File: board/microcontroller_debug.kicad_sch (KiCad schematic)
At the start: 1 part, among them J401 DBG

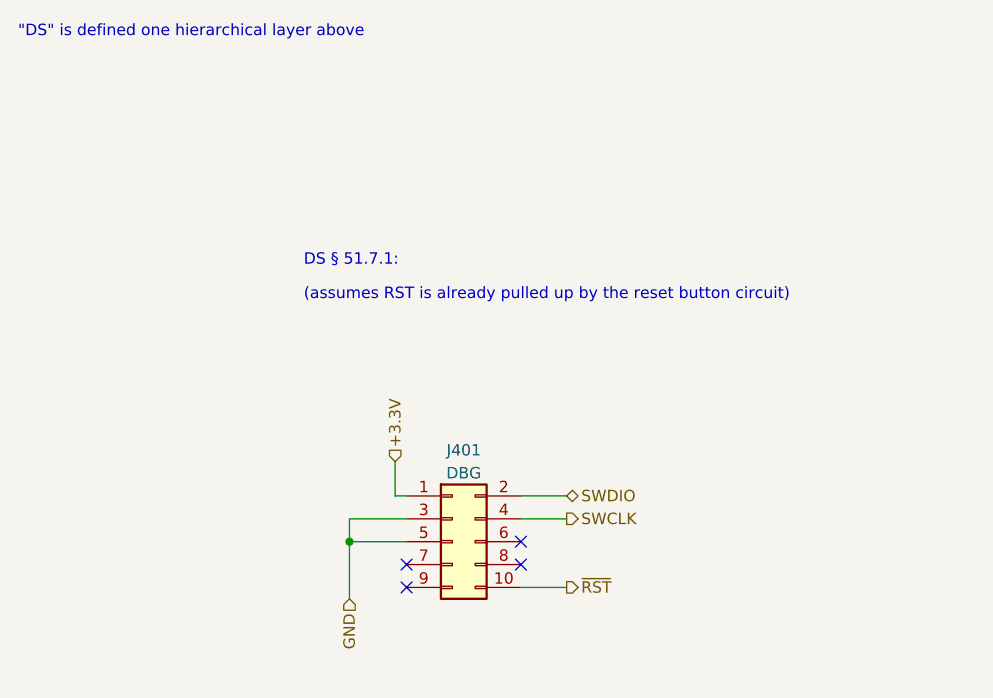
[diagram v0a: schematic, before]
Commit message: redo board with STM32G0B0CET
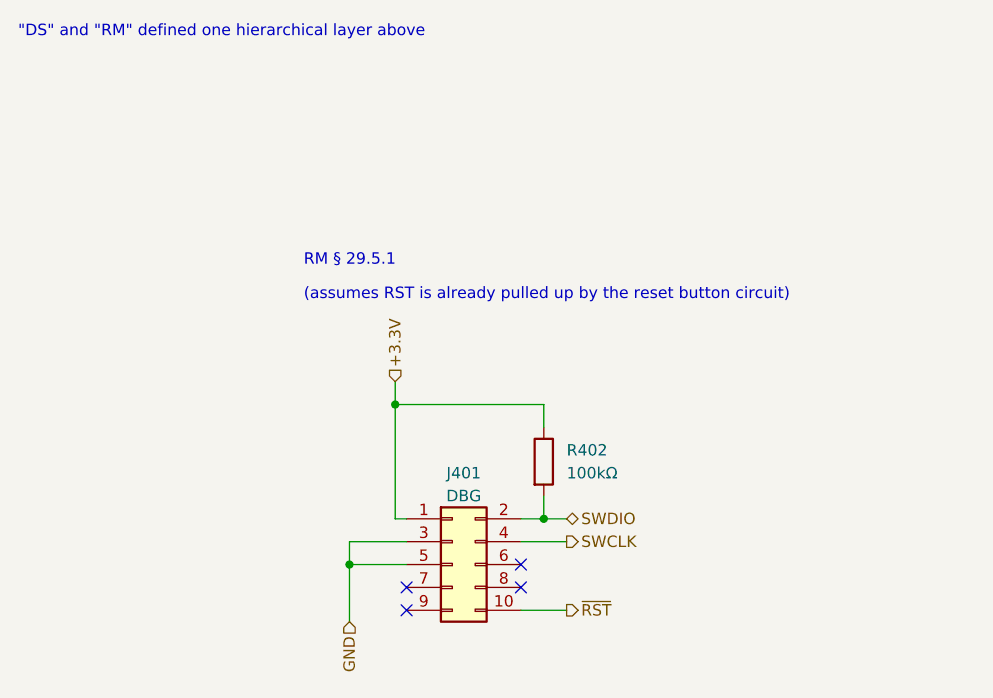
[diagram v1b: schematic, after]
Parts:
- added R402: 100kΩ, Resistor_SMD:R_0402_1005Metric, symbol Device:R
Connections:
- net +3.3V: now also R402.1
- net SWDIO: now also R402.2
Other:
- note added: ""DS" and "RM" defined one hierarchical layer above"
- note added: "RM § 29.5.1"
- note removed: ""DS" is defined one hierarchical layer above"
- note removed: "DS § 51.7.1:"
- moved on the sheet: J401
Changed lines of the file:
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@@
 (kicad_sch (version 20230121) (generator eeschema)
   (paper "A4")
-  (junction (at 50.8 72.39) (diameter 0) (color 0 0 0 0)
+  (junction (at 72.39 69.85) (diameter 0) (color 0 0 0 0)
   )
+  (junction (at 55.88 57.15) (diameter 0) (color 0 0 0 0)
+  )
+  (junction (at 50.8 74.93) (diameter 0) (color 0 0 0 0)
+  )
+  (no_connect (at 57.15 80.01))
+  (no_connect (at 69.85 77.47))
+  (no_connect (at 69.85 74.93))
   (no_connect (at 57.15 77.47))
-  (no_connect (at 69.85 74.93))
-  (no_connect (at 69.85 72.39))
-  (no_connect (at 57.15 74.93))
-  (wire (pts (xy 50.8 72.39) (xy 57.15 72.39))
+  (wire (pts (xy 72.39 57.15) (xy 72.39 59.69))
     (stroke (width 0) (type default))
   )
-  (wire (pts (xy 55.88 67.31) (xy 55.88 63.5))
+  (wire (pts (xy 50.8 74.93) (xy 57.15 74.93))
     (stroke (width 0) (type default))
   )
-  (wire (pts (xy 69.85 77.47) (xy 74.93 77.47))
+  (wire (pts (xy 55.88 57.15) (xy 72.39 57.15))
     (stroke (width 0) (type default))
   )
-  (wire (pts (xy 69.85 69.85) (xy 74.93 69.85))
+  (wire (pts (xy 55.88 54.61) (xy 55.88 57.15))
     (stroke (width 0) (type default))
   )
-  (wire (pts (xy 69.85 67.31) (xy 74.93 67.31))
+  (wire (pts (xy 69.85 80.01) (xy 74.93 80.01))
     (stroke (width 0) (type default))
   )
-  (wire (pts (xy 57.15 69.85) (xy 50.8 69.85))
+  (wire (pts (xy 69.85 72.39) (xy 74.93 72.39))
     (stroke (width 0) (type default))
   )
-  (wire (pts (xy 57.15 67.31) (xy 55.88 67.31))
+  (wire (pts (xy 69.85 69.85) (xy 72.39 69.85))
     (stroke (width 0) (type default))
   )
-  (wire (pts (xy 50.8 69.85) (xy 50.8 72.39))
+  (wire (pts (xy 55.88 57.15) (xy 55.88 69.85))
     (stroke (width 0) (type default))
   )
-  (wire (pts (xy 50.8 72.39) (xy 50.8 78.74))
+  (wire (pts (xy 57.15 72.39) (xy 50.8 72.39))
     (stroke (width 0) (type default))
   )
-  (text "DS § 51.7.1:" (at 45.72 41.91 0)
+  (wire (pts (xy 57.15 69.85) (xy 55.88 69.85))
+    (stroke (width 0) (type default))
+  )
+  (wire (pts (xy 72.39 69.85) (xy 74.93 69.85))
+    (stroke (width 0) (type default))
+  )
+  (wire (pts (xy 50.8 72.39) (xy 50.8 74.93))
+    (stroke (width 0) (type default))
+  )
+  (wire (pts (xy 72.39 67.31) (xy 72.39 69.85))
+    (stroke (width 0) (type default))
+  )
+  (wire (pts (xy 50.8 74.93) (xy 50.8 81.28))
+    (stroke (width 0) (type default))
+  )
+  (text "RM § 29.5.1" (at 45.72 41.91 0)
     (effects (font (size 1.27 1.27)) (justify left bottom))
   )
@@
     (effects (font (size 1.27 1.27)) (justify left bottom))
   )
-  (text "\"DS\" is defined one hierarchical layer above" (at 13.97 16.51 0)
+  (text "\"DS\" and \"RM\" defined one hierarchical layer above"
+    (at 13.97 16.51 0)
     (effects (font (size 1.27 1.27)) (justify left bottom))
   )
-  (hierarchical_label "SWDIO" (shape bidirectional) (at 74.93 67.31 0) (fields_autoplaced)
+  (hierarchical_label "SWDIO" (shape bidirectional) (at 74.93 69.85 0) (fields_autoplaced)
     (effects (font (size 1.27 1.27)) (justify left))
   )
-  (hierarchical_label "SWCLK" (shape output) (at 74.93 69.85 0) (fields_autoplaced)
+  (hierarchical_label "SWCLK" (shape output) (at 74.93 72.39 0) (fields_autoplaced)
     (effects (font (size 1.27 1.27)) (justify left))
   )
-  (hierarchical_label "~{RST}" (shape output) (at 74.93 77.47 0) (fields_autoplaced)
+  (hierarchical_label "~{RST}" (shape output) (at 74.93 80.01 0) (fields_autoplaced)
     (effects (font (size 1.27 1.27)) (justify left))
   )
-  (hierarchical_label "+3.3V" (shape input) (at 55.88 63.5 90) (fields_autoplaced)
+  (hierarchical_label "+3.3V" (shape input) (at 55.88 54.61 90) (fields_autoplaced)
     (effects (font (size 1.27 1.27)) (justify left))
   )
-  (hierarchical_label "GND" (shape input) (at 50.8 78.74 270) (fields_autoplaced)
+  (hierarchical_label "GND" (shape input) (at 50.8 81.28 270) (fields_autoplaced)
     (effects (font (size 1.27 1.27)) (justify right))
   )
-  (symbol (lib_id "Connector_Generic:Conn_02x05_Odd_Even") (at 62.23 72.39 0) (unit 1)
+  (symbol (lib_id "Device:R") (at 72.39 63.5 0) (unit 1)
     (in_bom yes) (on_board yes) (dnp no) (fields_autoplaced)
-    (property "Reference" "J401" (at 63.5 62.23 0)
+    (property "Reference" "R402" (at 74.93 62.23 0)
+      (effects (font (size 1.27 1.27)) (justify left))
+    )
+    (property "Value" "100kΩ" (at 74.93 64.77 0)
+      (effects (font (size 1.27 1.27)) (justify left))
+    )
+    (property "Footprint" "Resistor_SMD:R_0402_1005Metric" (at 70.612 63.5 90)
+      (effects (font (size 1.27 1.27)) hide)
+    )
+    (property "Datasheet" "~" (at 72.39 63.5 0)
+      (effects (font (size 1.27 1.27)) hide)
+    )
+    (property "LCSC" "C25741" (at 72.39 63.5 0)
+      (effects (font (size 1.27 1.27)) hide)
+    )
+    (pin "1")
+    (pin "2")
+    (instances
+      (project "enocean-heater-control"
+        (path "/5b6b7d93-1453-4f42-9207-d781d45a3d31/6e36ffc7-833c-490a-a419-d98d15ce7ac1/cbeaf0f4-54d1-4064-b340-f318f51347e4"
+          (reference "R402") (unit 1)
+        )
+      )
+    )
+  )
+  (symbol (lib_id "Connector_Generic:Conn_02x05_Odd_Even") (at 62.23 74.93 0) (unit 1)
+    (in_bom yes) (on_board yes) (dnp no) (fields_autoplaced)
+    (property "Reference" "J401" (at 63.5 64.77 0)
       (effects (font (size 1.27 1.27)))
     )
-    (property "Value" "DBG" (at 63.5 64.77 0)
+    (property "Value" "DBG" (at 63.5 67.31 0)
       (effects (font (size 1.27 1.27)))
     )
-    (property "Footprint" "Connector_PinHeader_1.27mm:PinHeader_2x05_P1.27mm_Vertical_SMD" (at 62.23 72.39 0)
+    (property "Footprint" "Connector_PinHeader_1.27mm:PinHeader_2x05_P1.27mm_Vertical_SMD" (at 62.23 74.93 0)
       (effects (font (size 1.27 1.27)) hide)
     )
-    (property "Datasheet" "~" (at 62.23 72.39 0)
+    (property "Datasheet" "~" (at 62.23 74.93 0)
       (effects (font (size 1.27 1.27)) hide)
     )
-    (property "LCSC" "C5250218" (at 62.23 72.39 0)
+    (property "LCSC" "C5250218" (at 62.23 74.93 0)
       (effects (font (size 1.27 1.27)) hide)
     )
